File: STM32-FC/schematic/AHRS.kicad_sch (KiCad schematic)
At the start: 16 parts, among them U10 BMP390, U7 ICM-45686, U8 ICM-45686, U9 ICP-20100, U99 BMM350

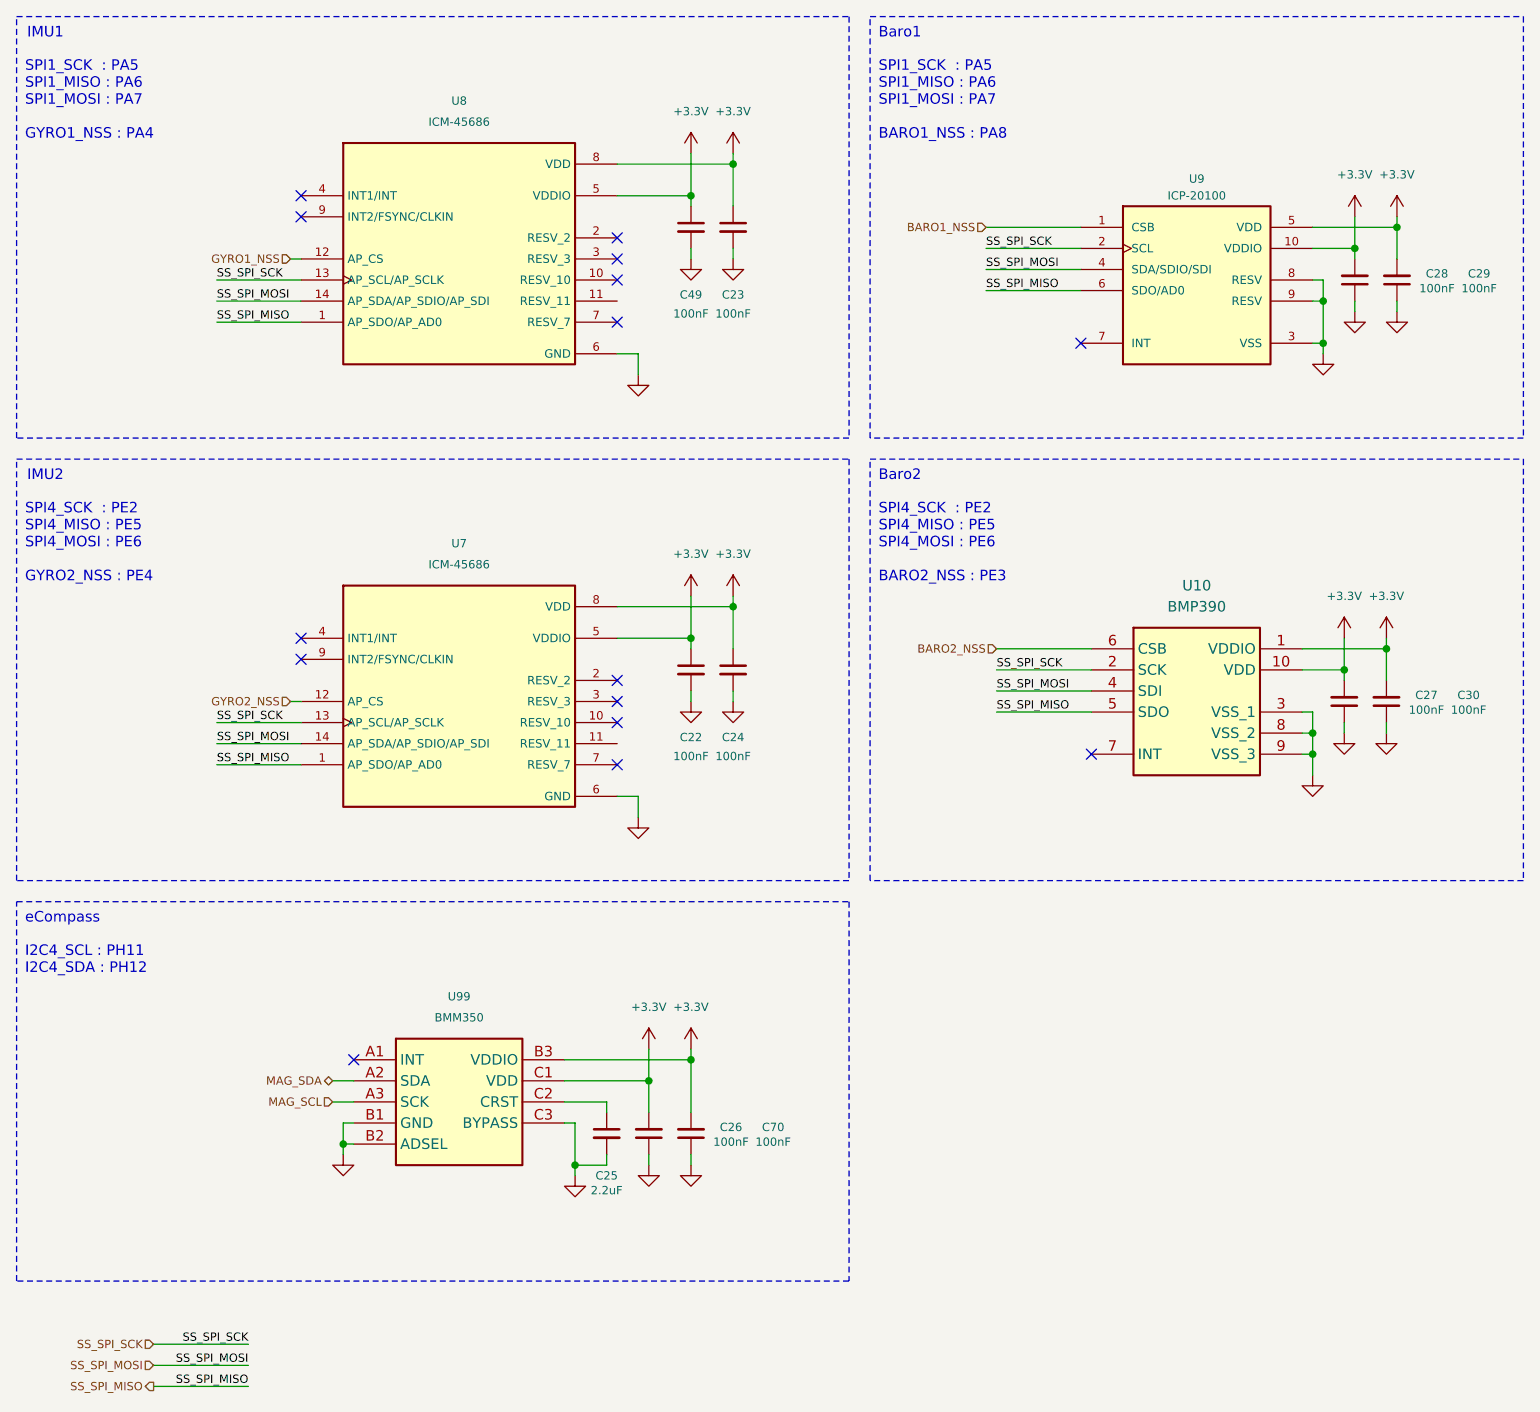
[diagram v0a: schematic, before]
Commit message: add basic circuit stm32f7
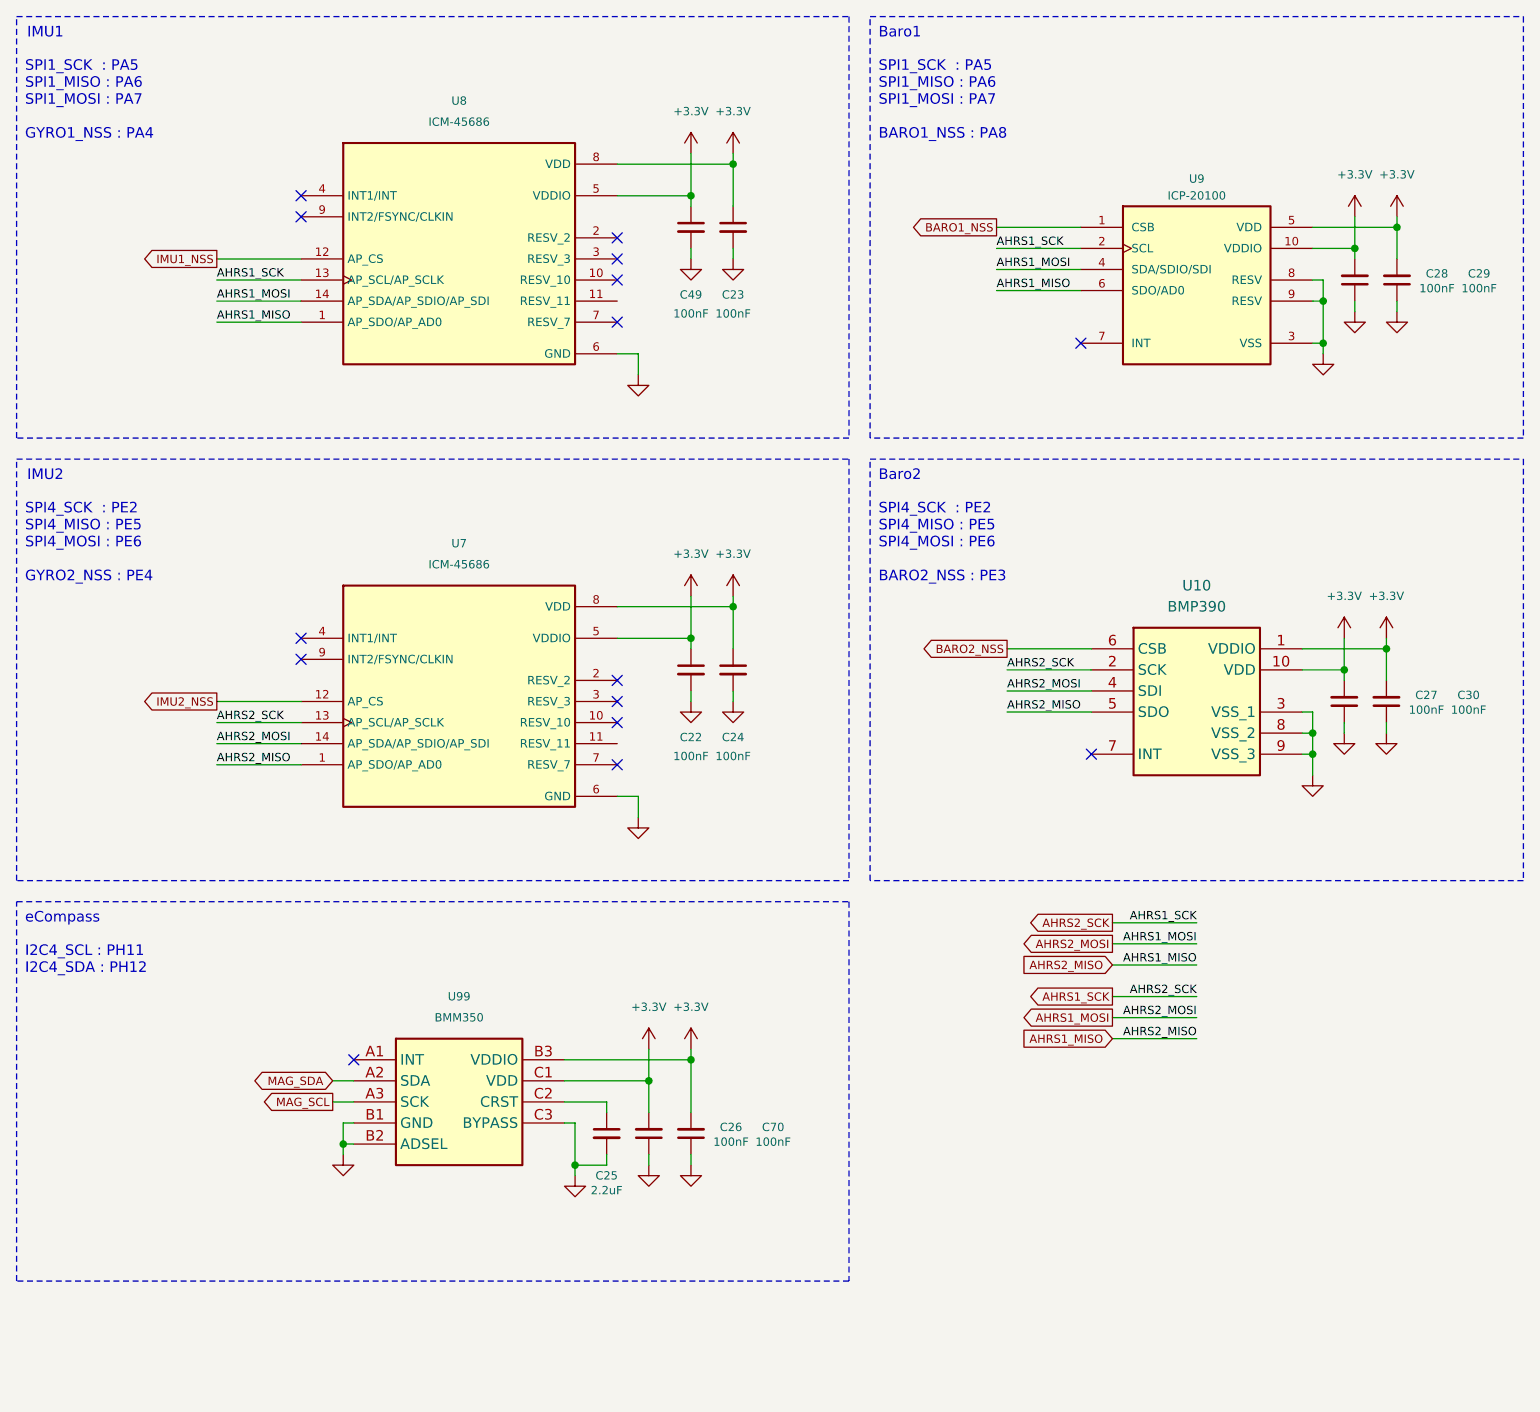
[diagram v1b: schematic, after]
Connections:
- net GYRO1_NSS renamed IMU1_NSS
- net GYRO2_NSS renamed IMU2_NSS
- net SS_SPI_MISO renamed AHRS1_MISO
- net SS_SPI_MOSI renamed AHRS1_MOSI
- net SS_SPI_SCK renamed AHRS1_SCK

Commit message: ERC passed
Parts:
- renumbered C25 to C36, C26 to C37, C49 to C38, C22 to C39, C70 to C40, C23 to C41, C24 to C42, C27 to C43, C28 to C44, C30 to C45, C29 to C46, U8 to U5, U7 to U6, U99 to U7, U9 to U8, U10 to U9
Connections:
- no-connect marks 15 -> 17
